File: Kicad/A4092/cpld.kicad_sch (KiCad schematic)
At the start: 16 parts, among them J2 Conn_01x06_Pin, U14 W25X40CLSN, U7 AMS1117-3.3, U9 XC95144XL-TQ144

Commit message: U14: Switch to wider SPI footprint
This will let builders use wide or small SPI flash parts.
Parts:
- U14: footprint Package_SO:SOIC-8_3.9x4.9mm_P1.27mm -> SOIC-8_multi:SOIC-8_multi
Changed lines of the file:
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@@
 			)
 		)
-		(property "Footprint" "Package_SO:SOIC-8_3.9x4.9mm_P1.27mm"
+		(property "Footprint" "SOIC-8_multi:SOIC-8_multi"
 			(at 212.09 19.05 0)
 			(effects

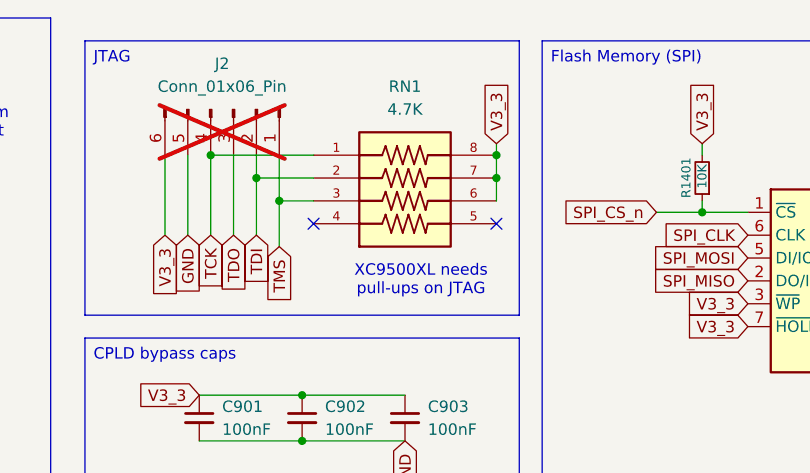
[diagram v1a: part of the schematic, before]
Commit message: Don't show DNP parts in 3D view
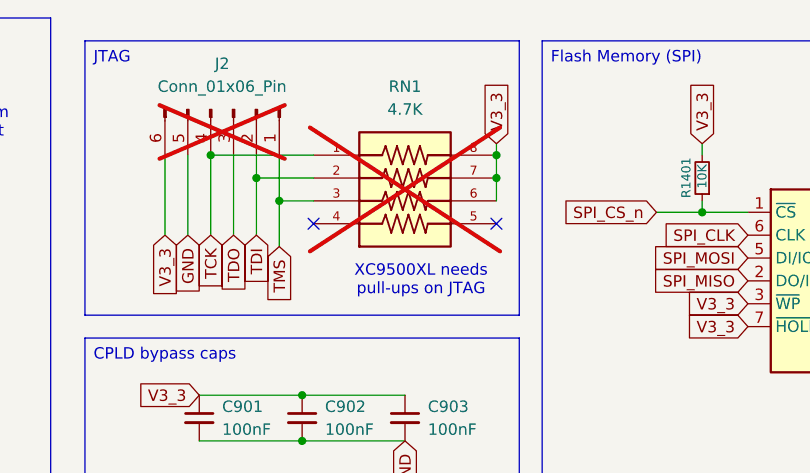
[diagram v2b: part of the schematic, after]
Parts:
- J2: now left out of the parts list
- RN1: now not fitted; now left out of the parts list
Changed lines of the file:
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@@
 		(unit 1)
 		(exclude_from_sim no)
-		(in_bom yes)
+		(in_bom no)
 		(on_board yes)
 		(dnp yes)
@@
 		(unit 1)
 		(exclude_from_sim no)
-		(in_bom yes)
-		(on_board yes)
-		(dnp no)
+		(in_bom no)
+		(on_board yes)
+		(dnp yes)
 		(fields_autoplaced yes)
 		(property "Reference" "RN1"

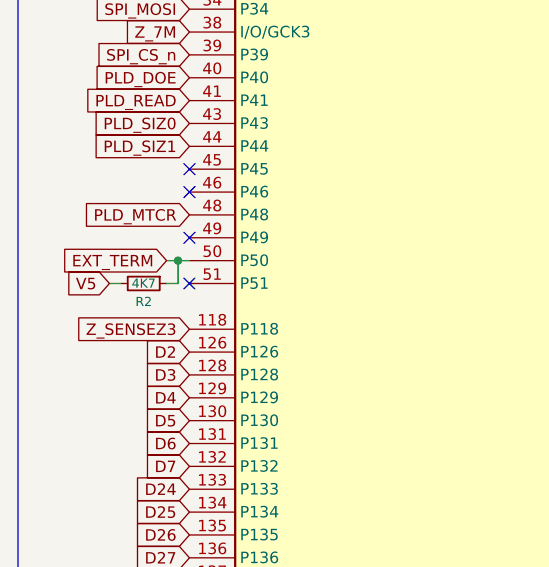
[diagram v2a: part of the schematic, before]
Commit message: Mark unneeded pull-up resistors DNP
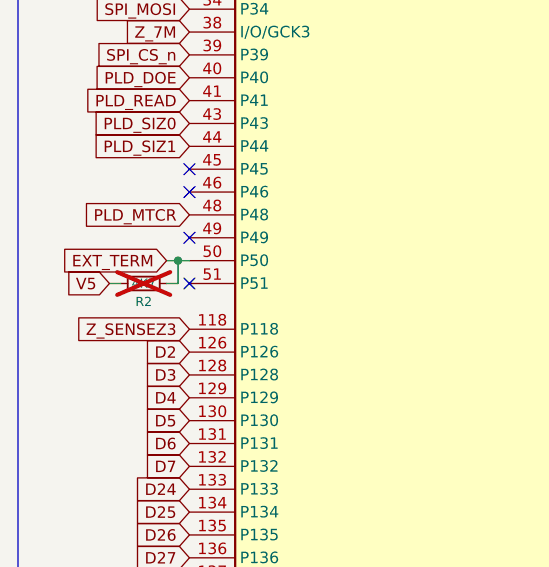
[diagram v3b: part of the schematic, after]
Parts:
- R2: now not fitted; now left out of the parts list
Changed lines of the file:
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@@
 		(unit 1)
 		(exclude_from_sim no)
-		(in_bom yes)
+		(in_bom no)
 		(on_board yes)
-		(dnp no)
+		(dnp yes)
 		(property "Reference" "R2"
 			(at 29.21 141.732 90)

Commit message: Fix footprint references in schematics
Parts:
- U9: footprint 144-TQFP_XIL -> XC95144XL_5TQG144C:144-TQFP_XIL
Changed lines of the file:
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@@
 			)
 		)
-		(property "Footprint" "144-TQFP_XIL"
+		(property "Footprint" "XC95144XL_5TQG144C:144-TQFP_XIL"
 			(at 67.31 104.14 0)
 			(effects
